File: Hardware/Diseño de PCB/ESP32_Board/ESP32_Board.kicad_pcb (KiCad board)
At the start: 2 copper layers, 82 x 65 mm, 9 parts, among them J1 Conn_02x15_Odd_Even, U1 ESP32 - DEVKIT, U2 logo

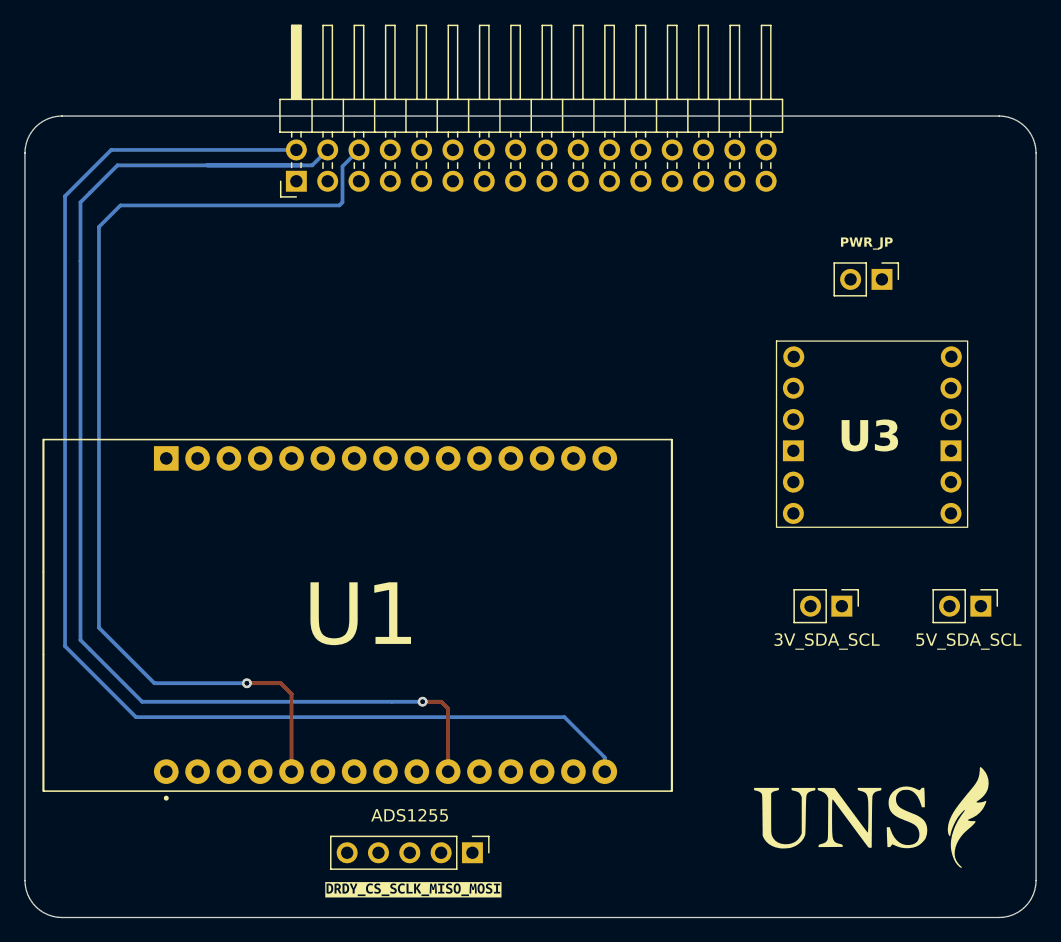
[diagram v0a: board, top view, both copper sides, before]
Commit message: Se resolvieron multiples incovenientes criticos en la interfaz y el backend. Principalmente, problemas que ralentizaban la lecturas de las muestras asociados con las graficas. Se agregaron tasas de refresco para los graficos para evitar actualizacion constante y saturación, sleep() al bucle del SerialWorker para evitar busy-wait al 100% y apertura y cierre unico de archivo de backup al principio y final del experimento (se estaba abriendo y cerrando por cada muestra leida). Además se resolvieron issues menores: método duplicado, np.asmatrix() deprecado, race condition en lectura de headers binarios, buffers O(n), import duplicado, path hardcodeado, autoRange que rompe el zoom manual, e inconsistencia LSV/CV en la nomenclatura.  Hardware: Se termino de diseñar la PCB de la ESP32, lista para fabricación. Firmware: small fixes.
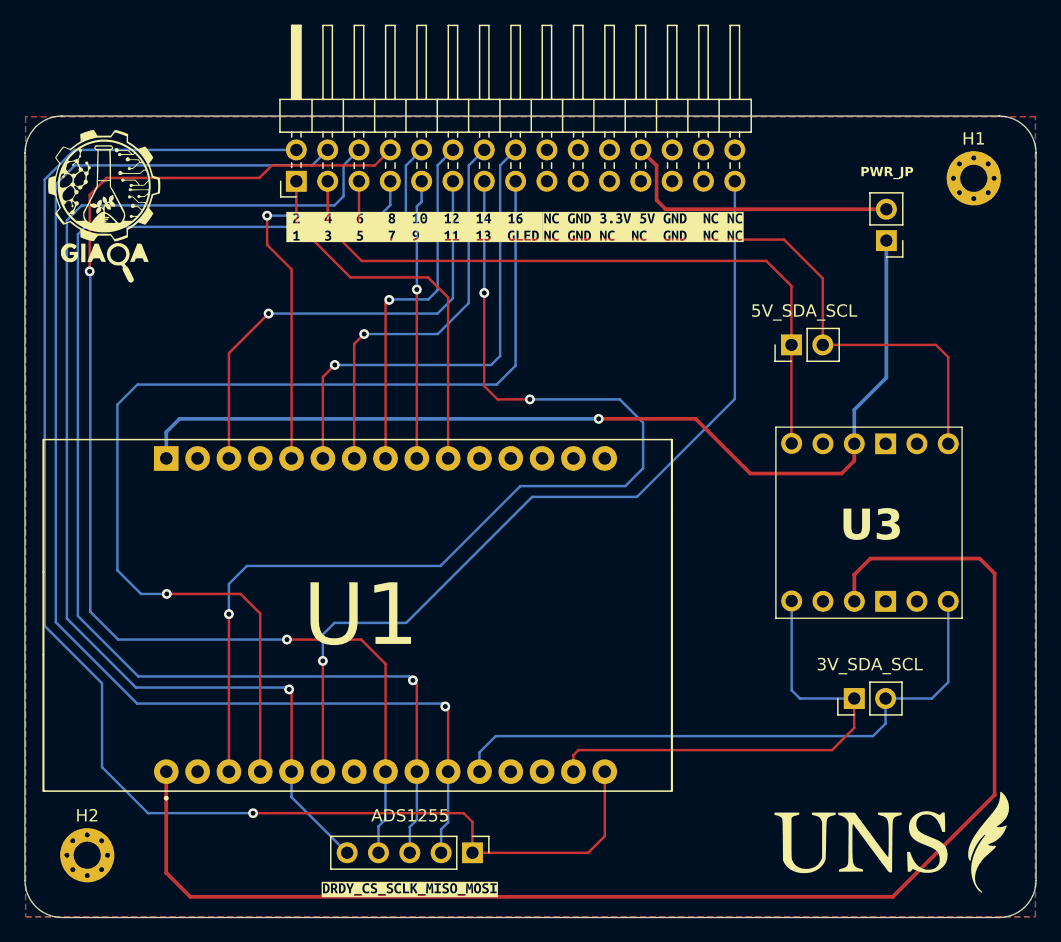
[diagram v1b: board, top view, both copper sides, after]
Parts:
- added H1: MountingHole_Pad, MountingHole:MountingHole_2.2mm_M2_Pad_Via, F.Cu at (172.4, 69.8)
- added H2: MountingHole_Pad, MountingHole:MountingHole_2.2mm_M2_Pad_Via, F.Cu at (100.5, 124.7)
- added kibuzzard-68F13266: G***, kibuzzard-68F13266, F.Cu at (145.7, 73.8)
- added kibuzzard-69A5AE09: G***, kibuzzard-69A5AE09, F.Cu at (127.1, 73.8)
- J1: footprint Connector_PinHeader_2.54mm:PinHeader_2x16_P2.54mm_Horizontal -> Connector_PinHeader_2.54mm:PinHeader_2x15_P2.54mm_Horizontal
- moved 5V_SDA_SCL 26.2 mm to (157.7, 83.3), turned to 90 degrees
- moved 3V_SDA_SCL 7.56 mm to (162.8, 112.0), turned to 90 degrees
- moved U3 7.18 mm to (164.2, 97.9), turned to 90 degrees
- moved PWR_JP 3.17 mm to (165.4, 74.8), turned to 180 degrees
- moved U2 2.59 mm to (166.2, 123.5)
- moved kibuzzard-69A1DE73 0.29 mm to (126.7, 127.5)
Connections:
- J1 pad 23: /5V -> unconnected-(J1-Pin_23-Pad23)
- J1 pad 24: unconnected-(J1-Pin_24-Pad24) -> /5V
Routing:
- net +3.3V: track 0.00 -> 112.2 mm
- net /ADS1255_SCLK: track 0.00 -> 107.7 mm, vias 0 -> 1
- net /ADS1255_CS: track 0.00 -> 101.0 mm, vias 0 -> 2
- net /GREEN_LED: track 0.00 -> 87.9 mm, vias 0 -> 1
- net /MAX4737_CE_EN: track 0.00 -> 87.0 mm, vias 0 -> 3
- net +5V: track 0.00 -> 79.6 mm, vias 0 -> 1
- net /ADS1255_CLOCK_PIN: track 0.00 -> 70.1 mm, vias 0 -> 1
- net /TO_DAC_SDA_PIN_5: track 0.00 -> 66.1 mm
- net /TO_DAC_SCL_PIN_3: track 0.00 -> 56.1 mm
- net /MAX_5217_SDA: track 0.00 -> 49.7 mm
- net /MAX_5217_SCL: track 0.00 -> 40.0 mm
- net /MAX4617_SEL_A: track 0.00 -> 39.1 mm, vias 0 -> 1
- net /MAX4737_WE_EN: track 0.00 -> 38.0 mm, vias 0 -> 1
- net /MAX4617_SEL_B: track 0.00 -> 32.9 mm, vias 0 -> 1
- net /MAX4737_CR_SHORT_EN: track 0.00 -> 32.8 mm, vias 0 -> 1
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- added copper zone on B.Cu, net GND
- added copper zone on F.Cu, net GND

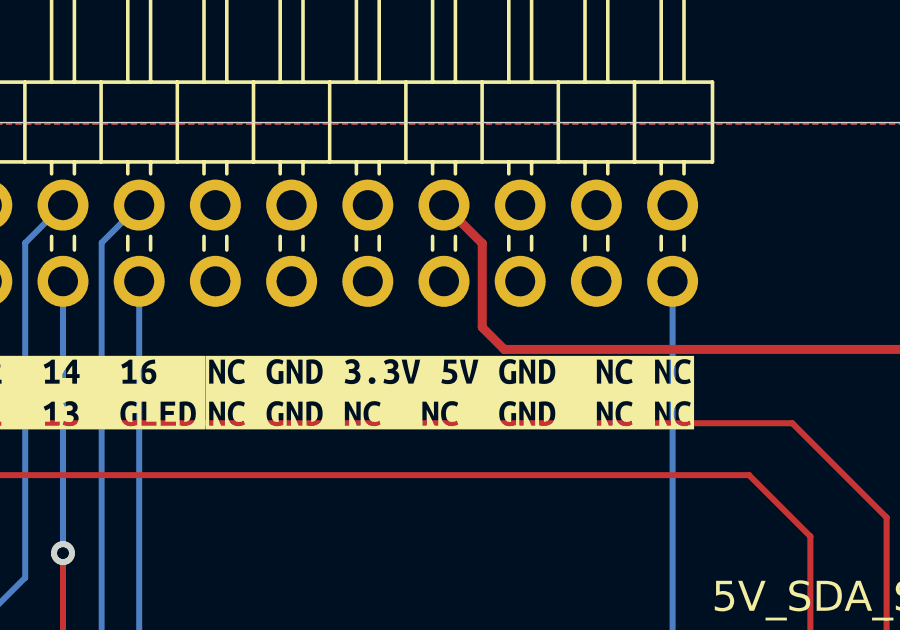
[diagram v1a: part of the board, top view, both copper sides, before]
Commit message: ESP32 Board 5V pinout correction
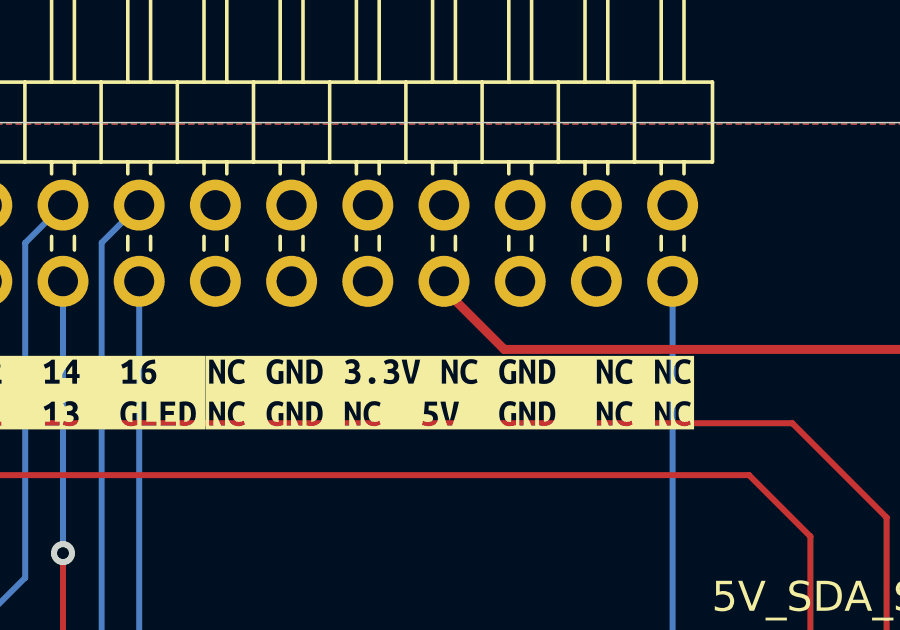
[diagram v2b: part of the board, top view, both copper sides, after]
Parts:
- removed kibuzzard-68F13266: G***, kibuzzard-68F13266
- added kibuzzard-69C42740: G***, kibuzzard-69C42740, F.Cu at (145.7, 73.8)
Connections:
- J1 pad 23: unconnected-(J1-Pin_23-Pad23) -> /5V
- J1 pad 24: /5V -> unconnected-(J1-Pin_24-Pad24)
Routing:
- net /5V: track 23.5 -> 21.0 mm
